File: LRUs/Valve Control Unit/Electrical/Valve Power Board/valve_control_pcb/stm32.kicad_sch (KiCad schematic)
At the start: 77 parts, among them J9 Conn_ST_STDC14, Q10 AO3400A, Q7 AO3400A, Q8 AO3400A, Q9 AO3400A, SW1 SW_SPDT, SW2 SW_Push, U12 STM32L496ZGT6, U30 W25Q128JVE, Y1 8MHz, Y2 32KHz

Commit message: Committttt
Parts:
- removed TP140, TP141, TP142, TP143, TP147, TP153, TP154: TestPoint, TestPoint:TestPoint_Pad_D1.0mm, symbol Connector:TestPoint
- BZ1: Pitch 10mm -> 9mmx9mm
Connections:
- net ADC_START: now reaches U12.49 (PF11)
- net ~{ADC_CS}: now reaches U12.40 (PA4)
- net ADC_SCLK: now reaches U12.41 (PA5)
- net ADC_MISO: now reaches U12.42 (PA6)
- net ADC_MOSI: now reaches U12.43 (PA7)
- net ~{ADC_RESET}: now reaches U12.46 (PB0)
- net ~{ADC_DRDY}: now reaches U12.50 (PF12)

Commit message: Commit da changes
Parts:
- removed TP139, TP144, TP145, TP148, TP150, TP159: TestPoint, TestPoint:TestPoint_Pad_D1.0mm, symbol Connector:TestPoint
- added TP153, TP154: TestPoint, TestPoint:TestPoint_Pad_D1.0mm, symbol Connector:TestPoint
- BZ1: JLCPCB Part # (none) -> C910763
- C101, C27, C28, C29, C30, C31, C32, C34, C35, C36, C37, C38, C39, C40, C41, C42, C43, C48, C49: footprint Capacitor_SMD:C_0402_1005Metric -> valve_pcb_footprints:C_0402_1005Metric
- C33, C45, C46: footprint Capacitor_SMD:C_0805_2012Metric -> valve_pcb_footprints:C_0805_2012Metric
- C44: footprint Capacitor_SMD:C_1206_3216Metric -> valve_pcb_footprints:C_1206_3216Metric
- C47: footprint Capacitor_SMD:C_0603_1608Metric -> valve_pcb_footprints:C_0603_1608Metric
- D25, D26, D27, D28: Vf 2V -> 3.1V
- J9: footprint Connector_PinHeader_1.27mm:PinHeader_2x07_P1.27mm_Vertical -> valve_pcb_footprints:SAMTEC_FTSH-107-01-X-DV-K; JLCPCB Part # (none) -> C5563894
- R100, R101, R102, R103, R104, R105, R106, R91, R92, R93, R94, R95, R96, R97, R98, R99: footprint Resistor_SMD:R_0603_1608Metric -> valve_pcb_footprints:R_0603_1608Metric
- SW1: JLCPCB Part # (none) -> C221829
- U30: footprint Package_SON:WSON-8-1EP_8x6mm_P1.27mm_EP3.4x4.3mm -> valve_pcb_footprints:WSON-8-1EP_8x6mm_P1.27mm_EP3.4x4.3mm
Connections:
- net QUADSPI_BK1_IO0: now also TP155.1
- net QUADSPI_BK1_IO1: now also TP156.1
- net QUADSPI_BK1_IO2: now also TP154.1
- net QUADSPI_BK1_IO3: now also TP153.1
- net QUADSPI_CLK: now also TP157.1
- net VALVE1.LSW_DIA_EN: now also U12.11 (PF1); no longer U12.119 (PD5)
- net VALVE1.LSW_LATCH: now also U12.2 (PE3); no longer U12.122 (PD6)
- net VALVE1.LSW_SEL1: now also U12.5 (PE6); no longer U12.117 (PD3)
- net VALVE1.LSW_SEL2: now also U12.10 (PF0); no longer U12.118 (PD4)
- net VALVE1.~{LSW_ST}: now also U12.3 (PE4); no longer U12.123 (PD7)
- net VALVE1_HSS_EN: now also U12.1 (PE2); no longer U12.115 (PD1)
- net VALVE1_LSS_EN: now also U12.4 (PE5); no longer U12.114 (PD0)
- net VALVE2.LSW_DIA_EN: now also U12.139 (PB8); no longer U12.132 (PG15)
- net VALVE2.LSW_LATCH: now also U12.135 (PB5); no longer U12.133 (PB3)
- net VALVE2.LSW_SEL1: now also U12.141 (PE0); no longer U12.126 (PG11)
- net VALVE2.LSW_SEL2: now also U12.140 (PB9); no longer U12.127 (PG12)
- net VALVE2.~{LSW_ST}: now also U12.137 (PB7); no longer U12.134 (PB4)
- net VALVE2_HSS_EN: now also U12.136 (PB6); no longer U12.125 (PG10)
- net VALVE2_LSS_EN: now also U12.142 (PE1); no longer U12.124 (PG9)
- net VALVE3.LSW_DIA_EN: now also U12.127 (PG12); no longer U12.140 (PB9)
- net VALVE3.LSW_LATCH: now also U12.124 (PG9); no longer U12.141 (PE0)
- net VALVE3.LSW_SEL1: now also U12.133 (PB3); no longer U12.137 (PB7)
- net VALVE3.LSW_SEL2: now also U12.132 (PG15); no longer U12.139 (PB8)
- net VALVE3.~{LSW_ST}: now also U12.126 (PG11); no longer U12.142 (PE1)
- net VALVE3_HSS_EN: now also U12.125 (PG10); no longer U12.136 (PB6)
- net VALVE3_LSS_EN: now also U12.134 (PB4); no longer U12.135 (PB5)
- net VALVE4.LSW_DIA_EN: now also U12.118 (PD4); no longer U12.5 (PE6)
- net VALVE4.LSW_LATCH: now also U12.114 (PD0); no longer U12.10 (PF0)
- net VALVE4.LSW_SEL1: now also U12.122 (PD6); no longer U12.3 (PE4)
- net VALVE4.LSW_SEL2: now also U12.119 (PD5); no longer U12.4 (PE5)
- net VALVE4.~{LSW_ST}: now also U12.117 (PD3); no longer U12.11 (PF1)
- net VALVE4_HSS_EN: now also U12.115 (PD1); no longer U12.2 (PE3)
- net VALVE4_LSS_EN: now also U12.123 (PD7); no longer U12.1 (PE2)
- net VALVE5.LSW_DIA_EN: now also U12.56 (PG0); no longer U12.55 (PF15)
- net VALVE5.LSW_LATCH: now also U12.59 (PE8); no longer U12.54 (PF14)
- net VALVE5.LSW_SEL1: now also U12.54 (PF14); no longer U12.57 (PG1)
- net VALVE5.LSW_SEL2: now also U12.55 (PF15); no longer U12.56 (PG0)
- net VALVE5.~{LSW_ST}: now also U12.57 (PG1); no longer U12.53 (PF13)
- net VALVE5_LSS_EN: now also U12.53 (PF13); no longer U12.59 (PE8)
- net VALVE6.LSW_DIA_EN: now also U12.65 (PE12); no longer U12.64 (PE11)
- net VALVE6.LSW_LATCH: now also U12.68 (PE15); no longer U12.63 (PE10)
- net VALVE6.LSW_SEL1: now also U12.63 (PE10); no longer U12.66 (PE13)
- net VALVE6.LSW_SEL2: now also U12.64 (PE11); no longer U12.65 (PE12)
- net VALVE6.~{LSW_ST}: now also U12.66 (PE13); no longer U12.60 (PE9)
- net VALVE6_LSS_EN: now also U12.60 (PE9); no longer U12.68 (PE15)
- net ~{QUADSPI_BK1_NCS}: now also TP158.1
- net TEMP_ALERT2: now reaches U12.88 (PG3)
- net TEMP_ALERT2: no longer TP156.1
- net TEMP_ALERT5: now reaches U12.102 (PA10)
- net EFUSE_IMON: now reaches U12.91 (PG6)
- net TEMP_ALERT4: now reaches U12.100 (PA8)
- net TEMP_ALERT1: now reaches U12.37 (PA3)
- net at R93.2, R94.2, U12.69 (PB10): now also TP161.1
- net VALVE_GLOBAL_CTRL: now reaches U12.7 (PC13)
- net TEMP_ALERT6: now reaches U12.70 (PB11)
- net TEMP_ALERT3: now reaches U12.87 (PG2)
- net TEMP_ALERT3: no longer TP155.1
- net 5V_MAIN_PG: now reaches U12.89 (PG4)
- net 5V_MAIN_PG: no longer TP157.1
- net EFUSE_PG: now reaches U12.90 (PG5)
- net EFUSE_PG: no longer TP158.1
- net at TP160.1: now also BZ1.1 (+), R93.1; no longer U12.92 (PG7)
- net I2C3_SDA: now reaches U12.93 (PG8)
- net I2C3_SDA: no longer TP161.1
- new net I2C3_SCL: U12.92 (PG7)
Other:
- note added: "19"
- note added: "21"
- note added: "22"
- note added: "23"
- note added: "24"
- note added: "3"
- note added: "31"
- note added: "32"
- note added: "9"
- moved on the sheet: C48, C49, R93

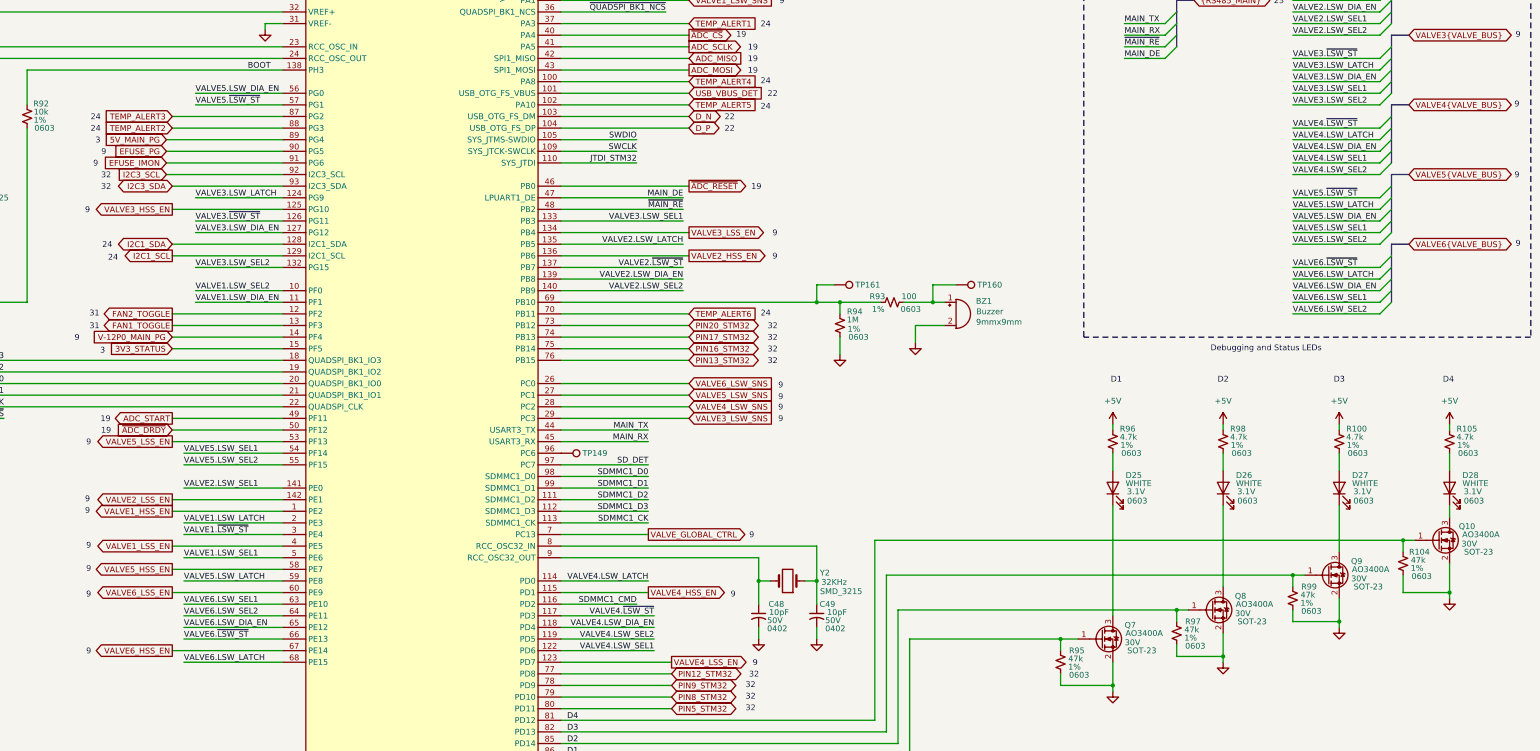
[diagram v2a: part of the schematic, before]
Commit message: Major changes due to architecture
Added battery muxing for valve power, igniter system, and separate system battery for control electronics
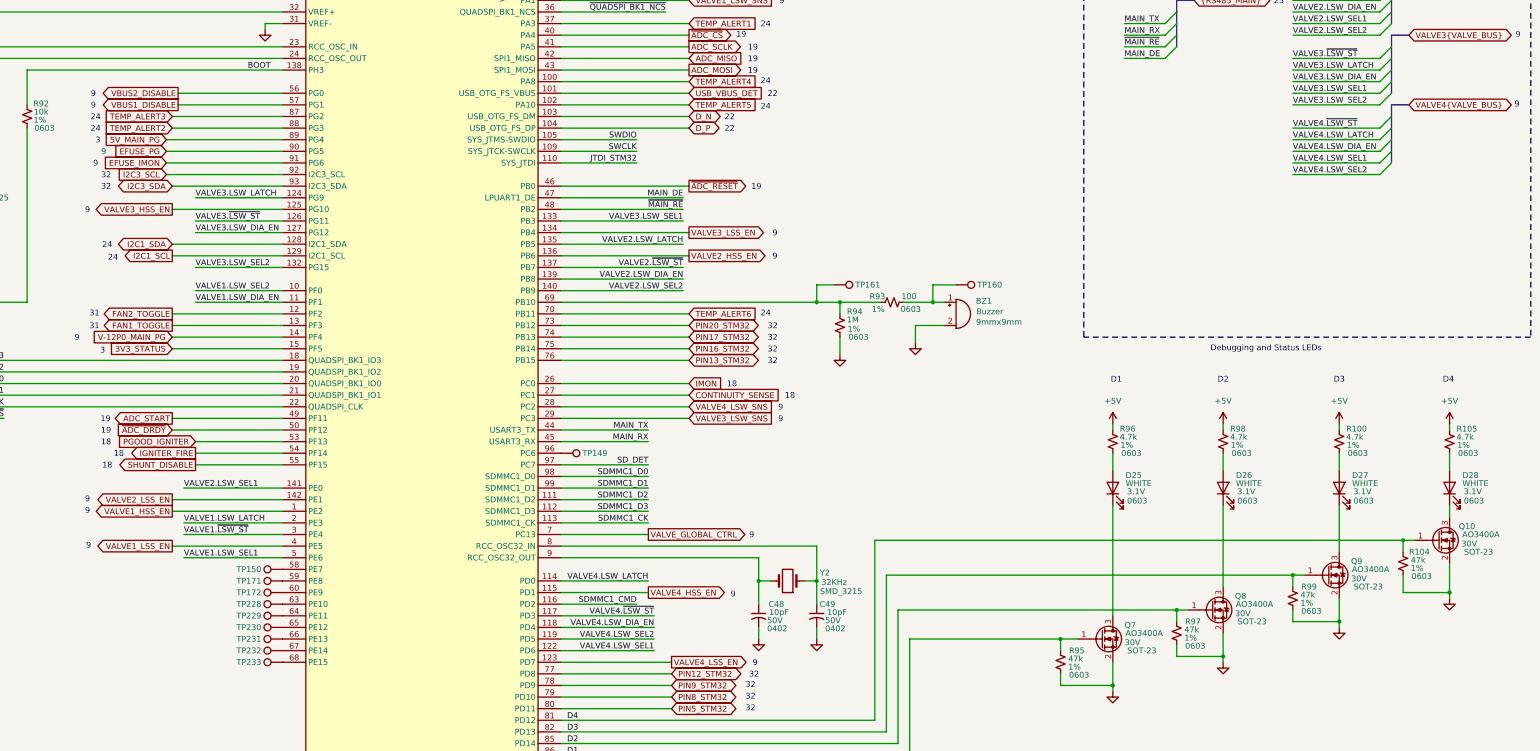
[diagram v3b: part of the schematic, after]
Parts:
- added TP150, TP171, TP172, TP228, TP229, TP230, TP231, TP232, TP233: TestPoint, TestPoint:TestPoint_Pad_D1.0mm, symbol Connector:TestPoint
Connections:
- net VALVE5.LSW_DIA_EN renamed VBUS2_DISABLE
- net VALVE5.LSW_LATCH: no longer names the net of U12.59 (PE8)
- net VALVE5.LSW_LATCH: now also TP171.1
- net VALVE5.LSW_SEL1 renamed IGNITER_FIRE
- net VALVE5.LSW_SEL2 renamed SHUNT_DISABLE
- net VALVE5.~{LSW_ST} renamed VBUS1_DISABLE
- net VALVE5_HSS_EN: no longer names the net of U12.58 (PE7)
- net VALVE5_HSS_EN: now also TP150.1
- net VALVE5_LSS_EN renamed PGOOD_IGNITER
- net VALVE5_LSW_SNS renamed CONTINUITY_SENSE
- net VALVE6.LSW_DIA_EN: no longer names the net of U12.65 (PE12)
- net VALVE6.LSW_DIA_EN: now also TP230.1
- net VALVE6.LSW_LATCH: no longer names the net of U12.68 (PE15)
- net VALVE6.LSW_LATCH: now also TP233.1
- net VALVE6.LSW_SEL1: no longer names the net of U12.63 (PE10)
- net VALVE6.LSW_SEL1: now also TP228.1
- net VALVE6.LSW_SEL2: no longer names the net of U12.64 (PE11)
- net VALVE6.LSW_SEL2: now also TP229.1
- net VALVE6.~{LSW_ST}: no longer names the net of U12.66 (PE13)
- net VALVE6.~{LSW_ST}: now also TP231.1
- net VALVE6_HSS_EN: no longer names the net of U12.67 (PE14)
- net VALVE6_HSS_EN: now also TP232.1
- net VALVE6_LSS_EN: no longer names the net of U12.60 (PE9)
- net VALVE6_LSS_EN: now also TP172.1
- net VALVE6_LSW_SNS renamed IMON
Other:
- note added: "18"

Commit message: Commit updates
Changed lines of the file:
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@@
 	(title_block
 		(title "STM32L496ZGT6")
-		(date "2026-08-27")
+		(date "2026-10-07")
 		(rev "A")
 	)
@@
 	(rectangle
 		(start 307.34 63.5)
-		(end 405.13 163.83)
+		(end 405.13 132.08)
 		(stroke
 			(width 0)

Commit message: Fixes
Added hops, fixed the planes, and fixed minor issues
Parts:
- renumbered C34 to C100, C36 to C101, C41 to C102, C38 to C103, C39 to C104, C40 to C105, C42 to C106, C43 to C107, C44 to C108, C45 to C109, C46 to C110, C47 to C111, C48 to C112, C49 to C113, C27 to C90, C30 to C91, C28 to C92, C33 to C93, C29 to C94, C35 to C95, C31 to C96, C101 to C97, C37 to C98, C32 to C99, D25 to D30, D26 to D31, D27 to D32, D28 to D33, J9 to J14, Q7 to Q15, Q8 to Q16, Q9 to Q17, Q10 to Q18, R91 to R180, R92 to R181, R94 to R182, R93 to R183, R95 to R184, R96 to R185, R97 to R186, R98 to R187, R99 to R188, R100 to R189, R101 to R190, R102 to R191, R103 to R192, R104 to R193, R106 to R194, R105 to R195, TP153 to TP116, TP154 to TP117, TP155 to TP118, TP156 to TP119, TP157 to TP120, TP158 to TP121, TP150 to TP122, TP171 to TP123, TP172 to TP124, TP228 to TP125, TP229 to TP126, TP230 to TP127, TP231 to TP128, TP232 to TP129, TP233 to TP130, TP149 to TP131, TP161 to TP132, TP160 to TP133, U30 to U18, U12 to U19
